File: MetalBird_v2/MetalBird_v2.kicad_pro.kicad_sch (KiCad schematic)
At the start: 57 parts, among them J1 SWD, J10 VTX Conn, J11 USB/UART DEBUG, J3 Conn_01x08, J7 ELRS Reciver, J9 Camera Conn, Q1 PMOS, SW1 SW_Push_Open, U1 STM32F411CEUx, U2 AMS1117-3.3, U3 MPU-6050, U4 BMP280, Y1 8MHz

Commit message: Schematics updates
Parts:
- added C11: 10nF, symbol Device:C
- added C7: 100nF, symbol Device:C
- C5: value 330nF -> 220nF
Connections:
- net at AP62200WU-1.2 (SW), C5.2, L1.1: now also C11.2, C7.2
- net at AP62200WU-1.6 (BST), C5.1: now also C11.1, C7.1
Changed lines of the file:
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@@
 	)
 	(junction
+		(at 74.93 160.02)
+		(diameter 0)
+		(color 0 0 0 0)
+	)
+	(junction
 		(at 88.9 167.64)
 		(diameter 0)
@@
 	)
 	(junction
+		(at 74.93 165.1)
+		(diameter 0)
+		(color 0 0 0 0)
+	)
+	(junction
 		(at 191.77 170.18)
 		(diameter 0)
@@
 	)
 	(junction
+		(at 67.31 160.02)
+		(diameter 0)
+		(color 0 0 0 0)
+	)
+	(junction
 		(at 165.1 170.18)
 		(diameter 0)
@@
 	)
 	(junction
+		(at 67.31 165.1)
+		(diameter 0)
+		(color 0 0 0 0)
+	)
+	(junction
 		(at 88.9 33.02)
 		(diameter 0)
@@
 	(wire
 		(pts
+			(xy 74.93 160.02) (xy 74.93 165.1)
+		)
+		(stroke
+			(width 0)
+			(type default)
+		)
+	)
+	(wire
+		(pts
 			(xy 264.16 60.96) (xy 264.16 62.23)
 		)
@@
 	(wire
 		(pts
+			(xy 67.31 160.02) (xy 67.31 165.1)
+		)
+		(stroke
+			(width 0)
+			(type default)
+		)
+	)
+	(wire
+		(pts
 			(xy 194.31 62.23) (xy 194.31 63.5)
 		)
@@
 	(wire
 		(pts
+			(xy 67.31 154.94) (xy 67.31 160.02)
+		)
+		(stroke
+			(width 0)
+			(type default)
+		)
+	)
+	(wire
+		(pts
 			(xy 133.35 97.79) (xy 134.62 97.79)
 		)
@@
 	(wire
 		(pts
+			(xy 74.93 154.94) (xy 74.93 160.02)
+		)
+		(stroke
+			(width 0)
+			(type default)
+		)
+	)
+	(wire
+		(pts
 			(xy 88.9 40.64) (xy 99.06 40.64)
 		)
@@
 	)
 	(symbol
+		(lib_id "Device:C")
+		(at 71.12 154.94 90)
+		(unit 1)
+		(body_style 1)
+		(exclude_from_sim no)
+		(in_bom yes)
+		(on_board yes)
+		(in_pos_files yes)
+		(dnp no)
+		(fields_autoplaced yes)
+		(property "Reference" "C11"
+			(at 71.12 147.32 90)
+			(show_name no)
+			(do_not_autoplace no)
+			(effects
+				(font
+					(size 1.27 1.27)
+				)
+			)
+		)
+		(property "Value" "10nF"
+			(at 71.12 149.86 90)
+			(show_name no)
+			(do_not_autoplace no)
+			(effects
+				(font
+					(size 1.27 1.27)
+				)
+			)
+		)
+		(property "Footprint" ""
+			(at 74.93 153.9748 0)
+			(hide yes)
+			(show_name no)
+			(do_not_autoplace no)
+			(effects
+				(font
+					(size 1.27 1.27)
+				)
+			)
+		)
+		(property "Datasheet" ""
+			(at 71.12 154.94 0)
+			(hide yes)
+			(show_name no)
+			(do_not_autoplace no)
+			(effects
+				(font
+					(size 1.27 1.27)
+				)
+			)
+		)
+		(property "Description" "Unpolarized capacitor"
+			(at 71.12 154.94 0)
+			(hide yes)
+			(show_name no)
+			(do_not_autoplace no)
+			(effects
+				(font
+					(size 1.27 1.27)
+				)
+			)
+		)
+		(pin "1"
+		)
+		(pin "2"
+		)
+		(instances
+			(project "MetalBird_v2.kicad_pro"
+				(path "/883a9ca3-f572-4a21-acce-bb921b8002d3"
+					(reference "C11")
+					(unit 1)
+				)
+			)
+		)
+	)
+	(symbol
 		(lib_id "power:PWR_FLAG")
 		(at 22.86 44.45 0)
@@
 	)
 	(symbol
+		(lib_id "Device:C")
+		(at 71.12 160.02 90)
+		(unit 1)
+		(body_style 1)
+		(exclude_from_sim no)
+		(in_bom yes)
+		(on_board yes)
+		(in_pos_files yes)
+		(dnp no)
+		(fields_autoplaced yes)
+		(property "Reference" "C7"
+			(at 71.12 152.4 90)
+			(show_name no)
+			(do_not_autoplace no)
+			(effects
+				(font
+					(size 1.27 1.27)
+				)
+			)
+		)
+		(property "Value" "100nF"
+			(at 71.12 154.94 90)
+			(show_name no)
+			(do_not_autoplace no)
+			(effects
+				(font
+					(size 1.27 1.27)
+				)
+			)
+		)
+		(property "Footprint" ""
+			(at 74.93 159.0548 0)
+			(hide yes)
+			(show_name no)
+			(do_not_autoplace no)
+			(effects
+				(font
+					(size 1.27 1.27)
+				)
+			)
+		)
+		(property "Datasheet" ""
+			(at 71.12 160.02 0)
+			(hide yes)
+			(show_name no)
+			(do_not_autoplace no)
+			(effects
+				(font
+					(size 1.27 1.27)
+				)
+			)
+		)
+		(property "Description" "Unpolarized capacitor"
+			(at 71.12 160.02 0)
+			(hide yes)
+			(show_name no)
+			(do_not_autoplace no)
+			(effects
+				(font
+					(size 1.27 1.27)
+				)
+			)
+		)
+		(pin "1"
+		)
+		(pin "2"
+		)
+		(instances
+			(project "MetalBird_v2.kicad_pro"
+				(path "/883a9ca3-f572-4a21-acce-bb921b8002d3"
+					(reference "C7")
+					(unit 1)
+				)
+			)
+		)
+	)
+	(symbol
 		(lib_id "Switch:SW_Push_Open")
 		(at 125.73 52.07 0)
@@
 			)
 		)
-		(property "Value" "330nF"
+		(property "Value" "220nF"
 			(at 71.12 160.02 90)
 			(show_name no)

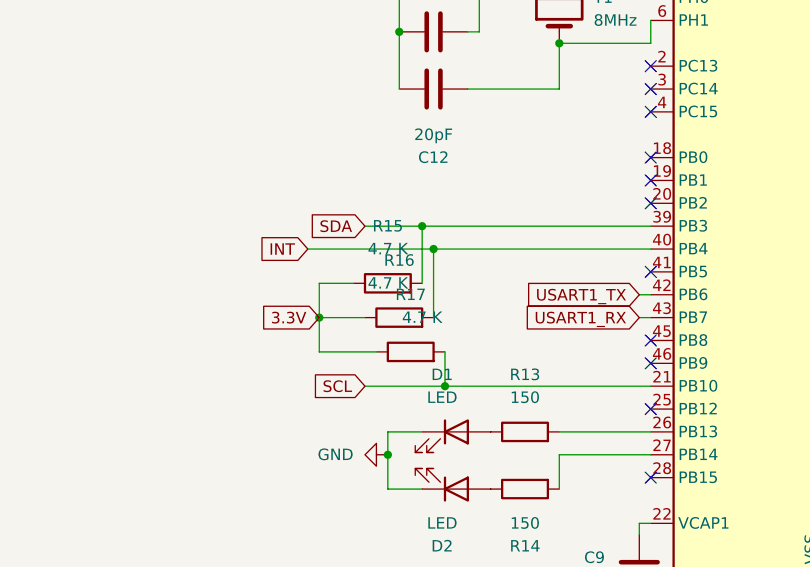
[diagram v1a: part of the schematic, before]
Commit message: I2C2 Initialization Bug fixes
1. Alternate Pin function in GPIO_MODER
2. External 2.2 K ohm pullup resistors (according to max RISE time)
3. Pin function Must be alternated before starting peripheral
4. Stack corruption in MACROS (Missing REG POPs)
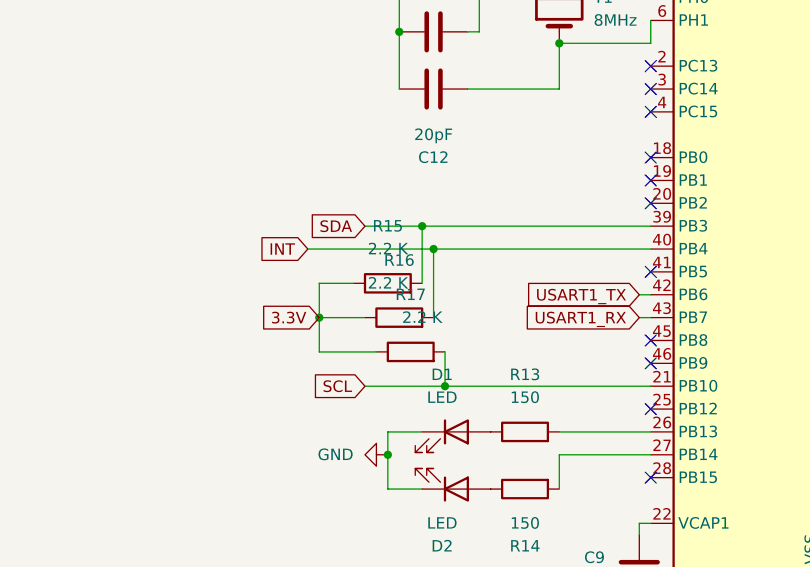
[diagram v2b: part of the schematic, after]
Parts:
- R15, R16, R17: value 4.7 K -> 2.2 K
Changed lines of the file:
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@@
 			)
 		)
-		(property "Value" "4.7 K"
+		(property "Value" "2.2 K"
 			(at 105.41 93.98 90)
 			(show_name no)
@@
 			)
 		)
-		(property "Value" "4.7 K"
+		(property "Value" "2.2 K"
 			(at 105.41 90.17 90)
 			(show_name no)
@@
 			)
 		)
-		(property "Value" "4.7 K"
+		(property "Value" "2.2 K"
 			(at 109.22 97.79 90)
 			(show_name no)
